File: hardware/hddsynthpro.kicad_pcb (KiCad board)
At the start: 4 copper layers, 85 x 76 mm, 48 parts, among them J1 USB-C, J2 5V in, J3 Link, J4 microSD, J5 IDE, J6 SWD, SW1 BOOTSEL, SW2 RESET, U1 PGA2350, U2 SN74CB3T3245PWR, U3 SN74CB3T3245PWR, U4 USBLC6-2SC6, U5 SN74CB3T3245PWR, U6 SN74CB3T3245PWR

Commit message: PCB rev 0.2: RP2350B on the board instead of the PGA2350 module
The PGA2350 is replaced by an RP2350B with Raspberry Pi's minimal-design
support circuit: their core regulator (polarity-marked inductor), 12 MHz
crystal, W25Q128 flash and USB 27R, with their regulator, QSPI and USB
layout copied relative to the VREG_LX pin; an AMS1117 makes 3V3. GPIO
numbers are unchanged. Supply pins each have a via under the chip.

Cheaper parts from the HDD Synth Mk5: HRO TYPE-C-31-M-12 USB-C, TS-1187A
buttons, and a generic TF PUSH microSD socket. The CB3T3245 bus switches
stay. Every symbol carries its LCSC part number, and Fabrication Toolkit
offsets where JLCPCB's footprint differs from KiCad's; jlcpcb.py applies
the same fitted corrections. check_netlist.py also checks the RP2350
support circuit. ERC and DRC are clean; parts for 5 boards about $68.50.

Co-Authored-By: Claude Opus 5.5 <noreply@anthropic.com>
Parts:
- added C10: 4.7uF, HDDSynthPro:C_0402_1005Metric_RPi_Wide, F.Cu at (143.0, 125.0)
- added C11: 4.7uF, Capacitor_SMD:C_0402_1005Metric, F.Cu at (145.2, 125.5)
- added C12: 100nF, Capacitor_SMD:C_0402_1005Metric, F.Cu at (129.6, 125.0)
- added C13: 100nF, Capacitor_SMD:C_0402_1005Metric, F.Cu at (133.6, 138.4)
- added C14: 100nF, Capacitor_SMD:C_0402_1005Metric, F.Cu at (133.6, 139.6)
- added C15: 100nF, Capacitor_SMD:C_0402_1005Metric, F.Cu at (137.4, 141.2)
- added C16: 100nF, Capacitor_SMD:C_0402_1005Metric, F.Cu at (146.4, 138.4)
- added C17: 100nF, Capacitor_SMD:C_0402_1005Metric, F.Cu at (146.8, 130.0)
- added C18: 100nF, Capacitor_SMD:C_0402_1005Metric, F.Cu at (146.6, 126.4)
- added C19: 100nF, Capacitor_SMD:C_0402_1005Metric, F.Cu at (126.4, 125.0)
- added C20: 100nF, Capacitor_SMD:C_0402_1005Metric, F.Cu at (128.0, 125.0)
- added C21: 100nF, Capacitor_SMD:C_0402_1005Metric, F.Cu at (146.4, 139.6)
- added C22: 100nF, Capacitor_SMD:C_0402_1005Metric, F.Cu at (148.0, 130.0)
- added C23: 100nF, Capacitor_SMD:C_0402_1005Metric, F.Cu at (147.8, 126.4)
- added C24: 100nF, Capacitor_SMD:C_0402_1005Metric, F.Cu at (123.2, 125.0)
- added C25: 100nF, Capacitor_SMD:C_0402_1005Metric, F.Cu at (124.8, 125.0)
- added C26: 100nF, Capacitor_SMD:C_0402_1005Metric, F.Cu at (137.2, 113.3)
- added C27: 15pF, Capacitor_SMD:C_0402_1005Metric, F.Cu at (136.6, 144.3)
- added C28: 15pF, Capacitor_SMD:C_0402_1005Metric, F.Cu at (143.4, 142.7)
- added C29: 10uF, Capacitor_SMD:C_0805_2012Metric, F.Cu at (165.0, 122.0)
- added C9: 4.7uF, HDDSynthPro:C_0402_1005Metric_RPi_Wide, F.Cu at (143.0, 125.9)
- added L1: 3.3uH, HDDSynthPro:L_Abracon_AOTA-B201610S3R3, F.Cu at (143.0, 123.3)
- added R16: 33, Resistor_SMD:R_0402_1005Metric, F.Cu at (145.2, 123.6)
- added R17: 1k, Resistor_SMD:R_0402_1005Metric, F.Cu at (141.6, 139.6)
- added R18: 10k, Resistor_SMD:R_0402_1005Metric, F.Cu at (134.0, 112.7)
- added R19: 1k, Resistor_SMD:R_0402_1005Metric, F.Cu at (129.9, 111.8)
- added R20: 1k, Resistor_SMD:R_0603_1608Metric, F.Cu at (154.0, 147.6)
- added R21: 27, Resistor_SMD:R_0402_1005Metric, F.Cu at (139.9, 123.1)
- added R22: 27, Resistor_SMD:R_0402_1005Metric, F.Cu at (140.9, 123.1)
- added U7: W25Q128JVSIQ, Package_SO:SOIC-8_5.3x5.3mm_P1.27mm, F.Cu at (134.1, 117.8)
- added U8: AMS1117-3.3, Package_TO_SOT_SMD:SOT-223-3_TabPin2, F.Cu at (172.0, 124.0)
- added Y1: 12MHz, Crystal:Crystal_SMD_3225-4Pin_3.2x2.5mm, F.Cu at (140.0, 143.5)
- J1: footprint Connector_USB:USB_C_Receptacle_GCT_USB4105-xx-A_16P_TopMnt_Horizontal -> Connector_USB:USB_C_Receptacle_HRO_TYPE-C-31-M-12
- J4: footprint Connector_Card:microSD_HC_Hirose_DM3AT-SF-PEJM5 -> HDDSynthPro:microSD_TF-PUSH
- SW1, SW2: footprint Button_Switch_SMD:SW_SPST_B3U-1000P -> Button_Switch_SMD:SW_Push_1P1T_XKB_TS-1187A
- U1: value PGA2350 -> RP2350B; footprint HDDSynthPro:PGA2350 -> Package_DFN_QFN:QFN-80-1EP_10x10mm_P0.4mm_EP3.4x3.4mm_ThermalVias
- moved SW2 47.3 mm to (158.5, 152.0)
- moved SW1 46.1 mm to (150.0, 152.0)
- moved C6 21.9 mm to (159.0, 121.0)
- moved R2 9.40 mm to (143.4, 110.2), turned to 180 degrees
- moved R1 9.20 mm to (150.4, 110.2), turned to 0 degrees
- moved U1 3.16 mm to (140.0, 132.0)
- moved U4 1.60 mm to (147.0, 112.6), turned to 90 degrees
- moved J4 0.76 mm to (175.3, 140.0)
- moved J1 0.54 mm to (147.0, 103.6)
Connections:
- net /PGA2350/LED_A renamed /RP2350/LED_A
- net /PGA2350/LINK_RX_EXT renamed /RP2350/LINK_RX_EXT
- net /PGA2350/LINK_TX_EXT renamed /RP2350/LINK_TX_EXT
- net /PGA2350/PWR_LED_A renamed /RP2350/PWR_LED_A
- C1 pad 1: VB -> /Power and USB/VB
- D1 pad 1: VB -> /Power and USB/VB
- D2 pad 1: VB -> /Power and USB/VB
- J4 pad 9: GND -> SD_CD
- R3 pad 1: /PGA2350/LINK_TX -> /RP2350/LINK_TX
- R4 pad 1: /PGA2350/LINK_RX -> /RP2350/LINK_RX
- R5 pad 1: /PGA2350/LED -> /RP2350/LED
- SW2 pad 1: RUN -> RUN_BTN
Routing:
- net /RP2350/LED: track 0.00 -> 60.5 mm, vias 0 -> 2
- net /RP2350/+1V1: track 0.00 -> 53.7 mm, vias 0 -> 9
- net VB: track 48.8 -> 0.00 mm, vias 1 -> 0
- net /Power and USB/VB: track 0.00 -> 47.9 mm, vias 0 -> 2
- net /RP2350/LINK_TX: track 0.00 -> 37.8 mm, vias 0 -> 2
- net +3V3: track 21.2 -> 54.5 mm, vias 20 -> 48
- net /PGA2350/LED: track 33.0 -> 0.00 mm, vias 1 -> 0
- net /RP2350/LINK_RX: track 0.00 -> 32.8 mm
- net BOOTSEL: track 29.8 -> 59.3 mm, vias 0 -> 2
- net /RP2350/QSPI_SS: track 0.00 -> 26.6 mm, vias 0 -> 2
- net /PGA2350/LINK_TX: track 25.5 -> 0.00 mm
- net SD_DAT0: track 26.9 -> 50.6 mm, vias 2 -> 3
- net SWCLK: track 27.1 -> 49.7 mm, vias 0 -> 1
- net /PGA2350/LINK_RX: track 19.5 -> 0.00 mm
- net GND: track 35.0 -> 54.4 mm, vias 30 -> 54
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- added copper zone on F.Cu, net +3V3
- added copper zone on F.Cu, net /RP2350/+1V1
- added copper zone on F.Cu, net /RP2350/VREG_LX
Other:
- board text added: "RP2350B IDE drive rev 0.2"
- board text removed: "PGA2350 IDE drive rev 0.1"

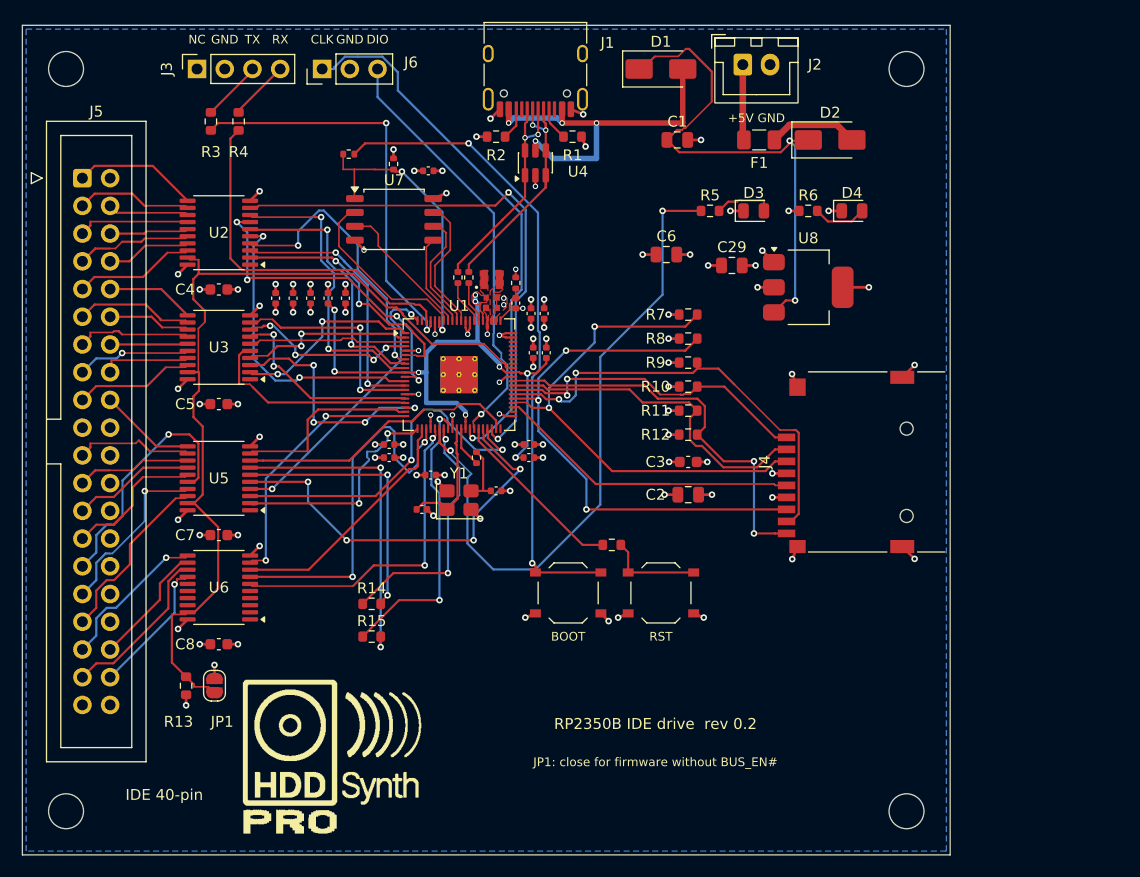
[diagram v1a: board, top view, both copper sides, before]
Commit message: PCB rev 0.3: HDD Synth Mk5 outline and holes, 5 V in on the link socket
- The board takes the Mk5's outline (100.33 x 69.88 mm, 2.54 mm corners)
  and its four M3 holes, so the two boards stack on standoffs. The IDE
  header moves inside the left-hand holes; everything else shifts right.
  The logo still fits on the front.
- J3 pin 1 takes 5 V from the HDD Synth through D5 (SS14) into VB, beside
  USB and the 5 V header, so one supply can run both boards. The Mk5's J6
  pin 1 is 3.3 V, so leave it unconnected with a Mk5.
- check_netlist.py checks the new input; rerouted with Freerouting: ERC 0,
  DRC 0 errors, 0 unconnected, 0 parity issues.

Co-Authored-By: Claude Opus 5.5 <noreply@anthropic.com>
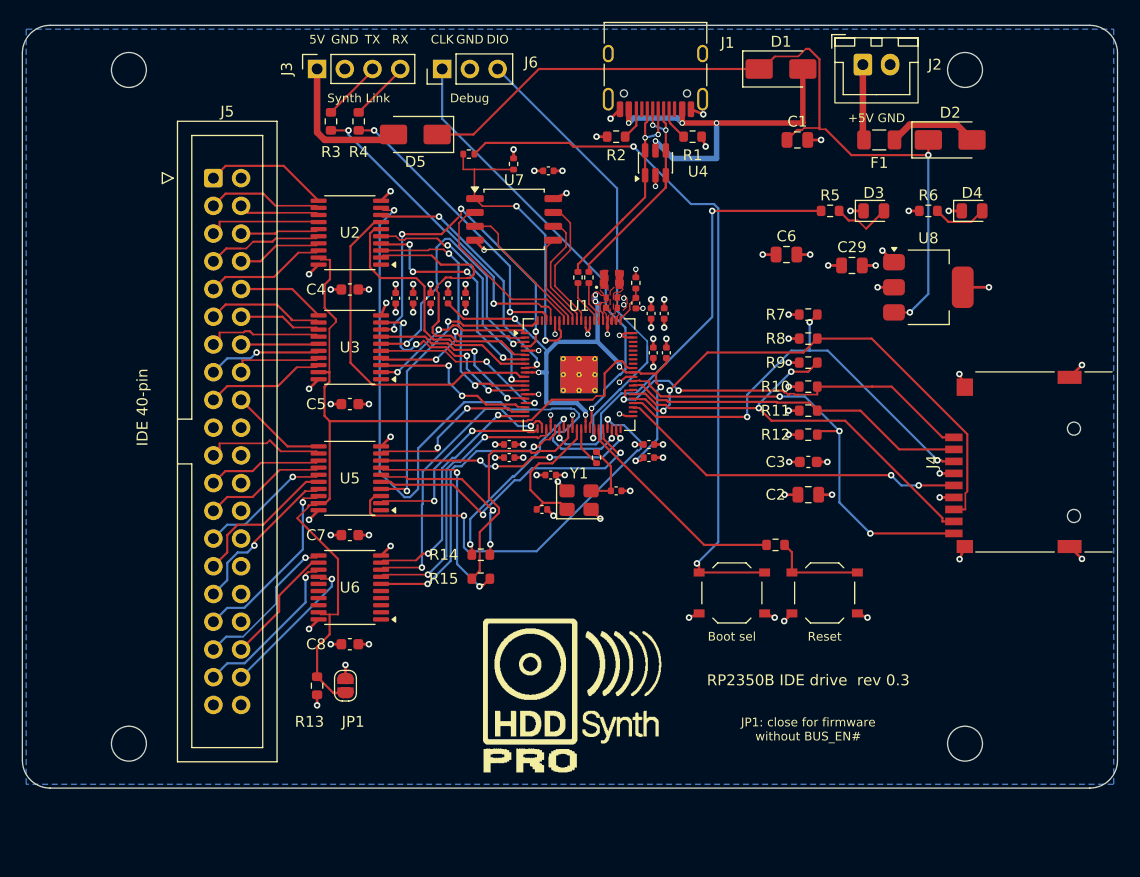
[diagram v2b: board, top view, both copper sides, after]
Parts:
- added D5: SS14, Diode_SMD:D_SMA, F.Cu at (136.0, 110.0)
- moved LOGO1 22.7 mm to (151.0, 161.2)
- moved J4 15.3 mm to (190.6, 140.0)
- moved R20 15.0 mm to (169.0, 147.6)
- moved SW1 15.0 mm to (165.0, 152.0)
- moved SW2 15.0 mm to (173.5, 152.0)
- moved C4 12.0 mm to (130.0, 124.2)
- moved C5 12.0 mm to (130.0, 134.7)
- moved C7 12.0 mm to (130.0, 146.7)
- moved C8 12.0 mm to (130.0, 156.7)
- moved J5 12.0 mm to (117.5, 114.0)
- moved JP1 12.0 mm to (129.6, 160.5)
- moved R13 12.0 mm to (127.0, 160.5)
- moved U2 12.0 mm to (130.0, 119.0)
- moved U3 12.0 mm to (130.0, 129.5)
- moved U5 12.0 mm to (130.0, 141.5)
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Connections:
- J3 pad 1: unconnected-(J3-Pin_1-Pad1) -> 5V_LINK
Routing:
- net /Power and USB/VB: track 47.9 -> 77.4 mm
- net /RP2350/LED: track 60.5 -> 41.0 mm
- net DD3: track 16.6 -> 33.1 mm
- net 5V_LINK: track 0.00 -> 13.3 mm
- net DD2: track 14.5 -> 27.2 mm, vias 0 -> 2
- net RESET_N: track 49.8 -> 62.2 mm
- net /IDE bus/DIOW_N_SW: track 29.4 -> 19.8 mm
- net /IDE bus/IDE_DMACK_N: track 23.1 -> 13.8 mm, vias 1 -> 0
- net /IDE bus/DIOR_N_SW: track 24.7 -> 15.8 mm
- net IORDY: track 37.6 -> 28.8 mm, vias 4 -> 2
- net CS0_N: track 34.5 -> 25.9 mm
- net SWCLK: track 49.7 -> 41.3 mm
- net /RP2350/LINK_TX: track 37.8 -> 29.6 mm
- net INTRQ: track 32.9 -> 39.6 mm
- net DD14: track 22.3 -> 15.7 mm, vias 4 -> 2
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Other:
- board size 85 x 76 mm -> 100.3 x 69.9 mm
- board text added: "5V"
- board text added: "Boot sel"
- board text added: "Debug"
- board text added: "RP2350B IDE drive rev 0.3"
- board text added: "Reset"
- board text added: "Synth Link"
- board text removed: "BOOT"
- board text removed: "NC"
- board text removed: "RP2350B IDE drive rev 0.2"
- board text removed: "RST"
